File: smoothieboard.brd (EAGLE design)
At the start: 105.1 x 105.1 mm, 236 parts, among them IC1 LPC1769, IC10 LM1117-3.3V, IC11 78L12F, IC2 A4982, IC3 A4982, IC4 MCP44X1, IC5 A4982, IC6 A4982, J10 POWER_JACKSMD, J5 POWER_JACKSMD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

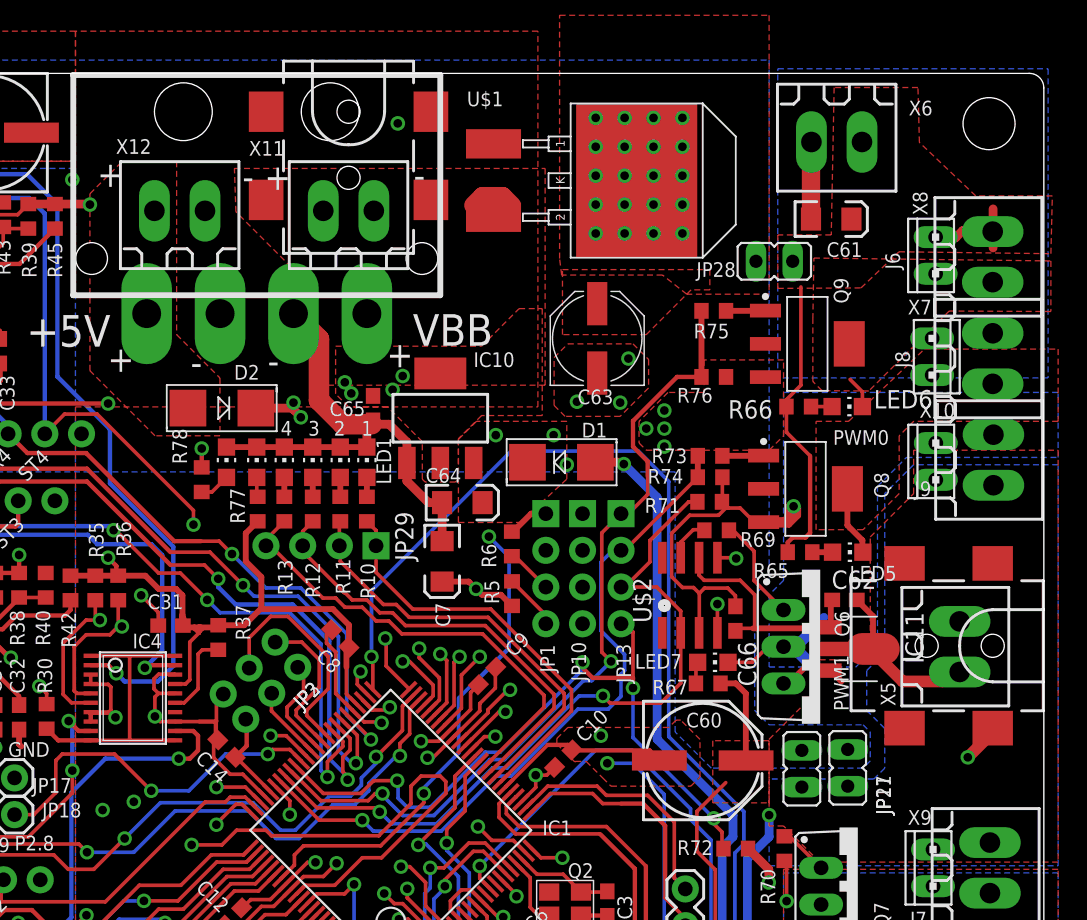
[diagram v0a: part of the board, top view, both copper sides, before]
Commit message: Removed Mosfet Driver Power SMD Jack
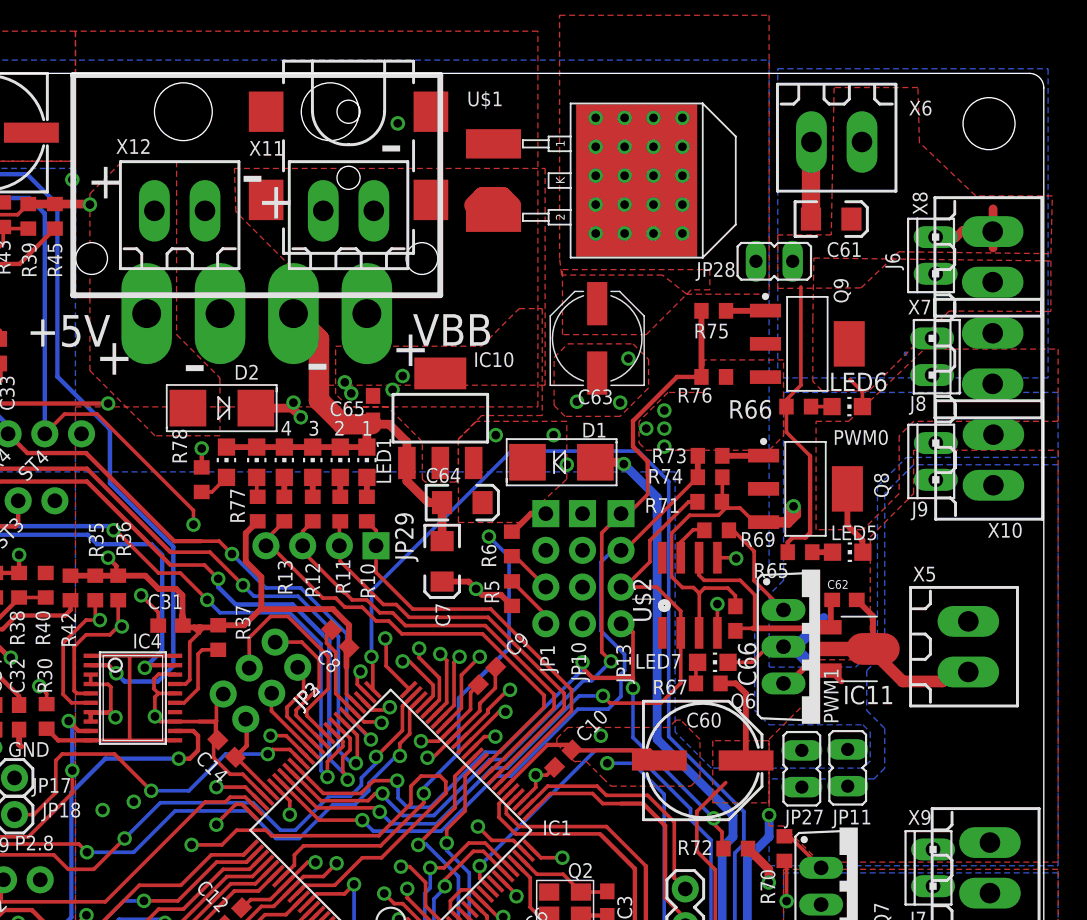
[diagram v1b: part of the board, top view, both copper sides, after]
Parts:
- removed J5: POWER_JACKSMD, SparkFun:POWER_JACK_SMD
- moved X5 0.60 mm to (99.8, 65.4)
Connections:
- net GND: no longer J5.VIN0
- net MOSFET_DRIVE: no longer J5.P$4
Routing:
- net GND: track 297.2 -> 294.4 mm, vias 234 -> 233

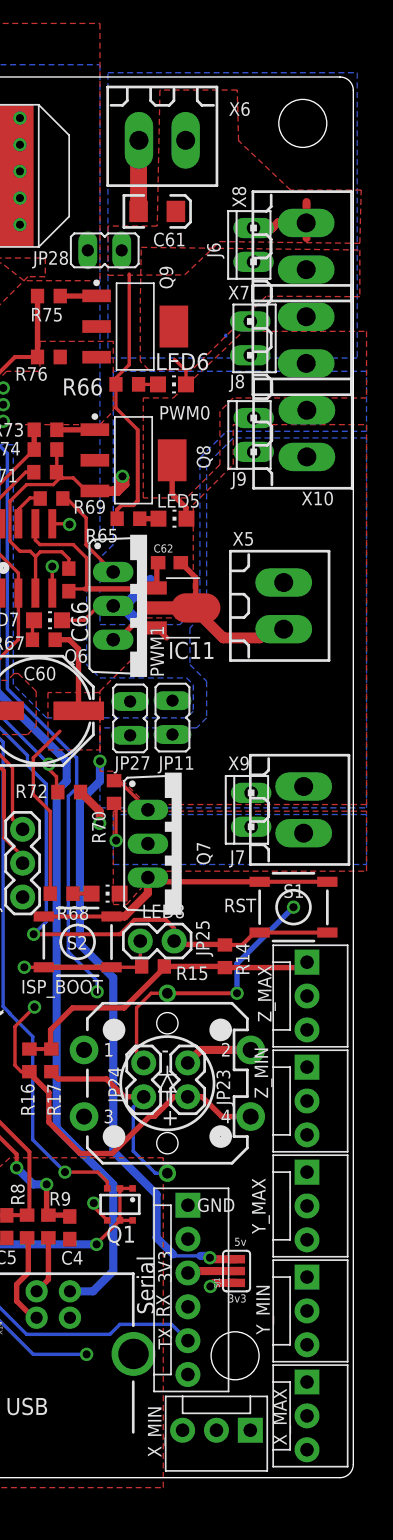
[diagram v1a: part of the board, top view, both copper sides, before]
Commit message: Removed second ground connection from IC11 (to improve MOSFET_DRIVE trace current handling)
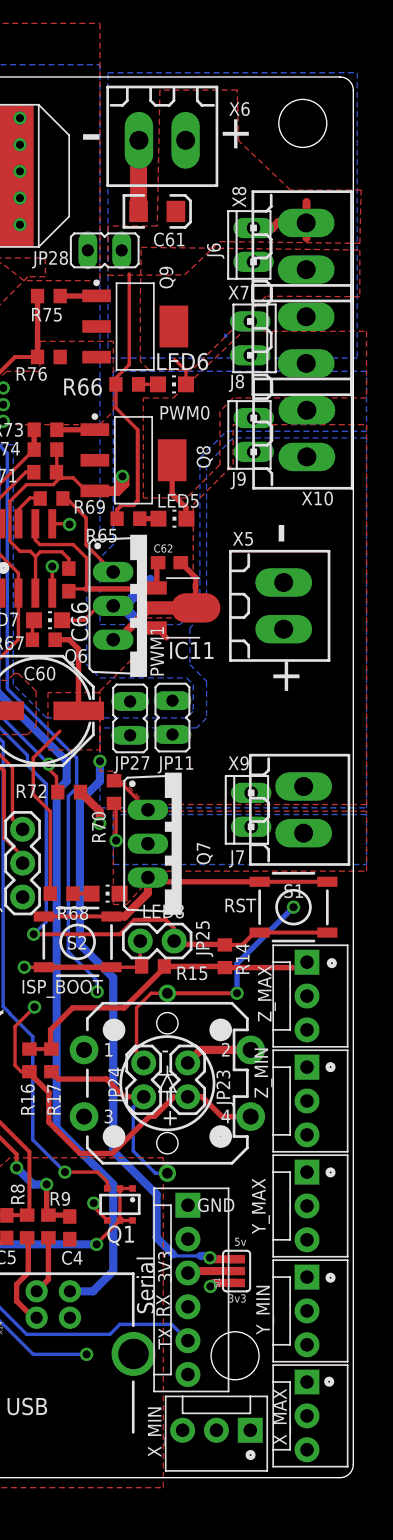
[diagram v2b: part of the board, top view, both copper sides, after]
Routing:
- net GND: track 294.4 -> 286.4 mm
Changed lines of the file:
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@@
 <setting verticaltext="up"/>
 </settings>
-<grid distance="0.1" unitdist="mm" unit="mm" style="dots" multiple="4" display="no" altdistance="0.0635" altunitdist="mm" altunit="mm"/>
+<grid distance="1" unitdist="mm" unit="mm" style="dots" multiple="4" display="no" altdistance="0.0635" altunitdist="mm" altunit="mm"/>
 <layers>
 <layer number="1" name="Top" color="4" fill="1" visible="yes" active="yes"/>
-<layer number="2" name="Route2" color="2" fill="1" visible="yes" active="yes"/>
+<layer number="2" name="Route2" color="2" fill="1" visible="no" active="yes"/>
 <layer number="3" name="Route3" color="4" fill="3" visible="no" active="no"/>
 <layer number="4" name="Route4" color="1" fill="4" visible="no" active="no"/>
@@
 <layer number="13" name="Route13" color="4" fill="5" visible="no" active="no"/>
 <layer number="14" name="Route14" color="1" fill="6" visible="no" active="no"/>
-<layer number="15" name="Route15" color="5" fill="1" visible="yes" active="yes"/>
+<layer number="15" name="Route15" color="5" fill="1" visible="no" active="yes"/>
 <layer number="16" name="Bottom" color="1" fill="1" visible="yes" active="yes"/>
 <layer number="17" name="Pads" color="2" fill="1" visible="yes" active="yes"/>
@@
 <text x="45.402" y="83.251" size="3.81" layer="25">-</text>
 <text x="53.902" y="83.351" size="3.81" layer="25">-</text>
+<circle x="97.3" y="1.7" radius="0.22360625" width="0.3048" layer="25"/>
+<circle x="103.2" y="7.2" radius="0.22360625" width="0.3048" layer="25"/>
+<circle x="103.3" y="15" radius="0.22360625" width="0.3048" layer="25"/>
+<circle x="103.3" y="22.9" radius="0.22360625" width="0.3048" layer="25"/>
+<circle x="103.3" y="30.8" radius="0.22360625" width="0.3048" layer="25"/>
+<circle x="103.4" y="38.6" radius="0.22360625" width="0.3048" layer="25"/>
+<text x="98.677" y="59.027" size="2.54" layer="25">+</text>
+<text x="101.049" y="70.002" size="3.81" layer="25" rot="R90">-</text>
+<text x="94.877" y="99.727" size="2.54" layer="25">+</text>
+<text x="84.502" y="99.151" size="3.81" layer="25">-</text>
 </plain>
 <attributes>
@@
 <wire x1="93.19" y1="65.25" x2="93.19" y2="67.5165" width="0.4064" layer="1"/>
 <wire x1="93.19" y1="67.5165" x2="92.0645" y2="68.642" width="0.4064" layer="1"/>
-<wire x1="93.19" y1="65.25" x2="93" y2="65.25" width="0.4064" layer="1"/>
-<wire x1="93" y1="65.25" x2="90.523" y2="65.25" width="0.4064" layer="1"/>
+<wire x1="93.19" y1="65.25" x2="90.523" y2="65.25" width="0.4064" layer="1"/>
 <wire x1="90.523" y1="65.25" x2="89.75" y2="65.25" width="0.4064" layer="1"/>
-<wire x1="89.75" y1="65.25" x2="87.365" y2="62.865" width="0.4064" layer="1"/>
-<wire x1="86.995" y1="62.865" x2="87.365" y2="62.865" width="0.4064" layer="1"/>
+<wire x1="89.75" y1="65.25" x2="87.365" y2="62.865" width="0.6096" layer="1"/>
+<wire x1="86.995" y1="62.865" x2="87.365" y2="62.865" width="0.6096" layer="1"/>
 <wire x1="68.58" y1="24.218" x2="68.58" y2="26.6065" width="0.6096" layer="1"/>
 <wire x1="68.58" y1="26.6065" x2="67.1195" y2="28.067" width="0.6096" layer="1"/>
@@
 <wire x1="85.979" y1="49.0855" x2="85.979" y2="49.999" width="0.6096" layer="1"/>
 <wire x1="85.979" y1="49.999" x2="84.543" y2="51.435" width="0.6096" layer="1"/>
-<wire x1="99.787" y1="63.655" x2="98.655" y2="63.655" width="0.8128" layer="1"/>
-<wire x1="98.655" y1="63.655" x2="98" y2="63" width="0.8128" layer="1"/>
-<wire x1="98" y1="63" x2="95.25" y2="63" width="0.8128" layer="1"/>
-<wire x1="95.25" y1="63" x2="93" y2="65.25" width="0.8128" layer="1"/>
 <via x="60.3045" y="101.619" extent="1-16" drill="0.6" diameter="1.016"/>
 <polygon width="0.8128" layer="1" rank="6">

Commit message: Fixed MOSFET labels on schematic to match BOM
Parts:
- Q6, Q7: value IRF540 -> AOT240L
- Q8, Q9: value BSP100 -> ZXMN4A06GTA
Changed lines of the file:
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@@
 <attribute name="VALUE" x="49.9745" y="73.406" size="1.27" layer="27" rot="R270"/>
 </element>
-<element name="Q6" library="transistor-power" package="TO220BV" value="IRF540" x="89.535" y="65.405" smashed="yes" rot="R270">
+<element name="Q6" library="transistor-power" package="TO220BV" value="AOT240L" x="89.535" y="65.405" smashed="yes" rot="R270">
 <attribute name="NAME" x="83.3185" y="61.1383" size="1.016" layer="25" ratio="10"/>
 <attribute name="VALUE" x="81.915" y="70.485" size="1.27" layer="27" ratio="10" rot="R270"/>
 </element>
-<element name="Q7" library="transistor-power" package="TO220BV" value="IRF540" x="92.1385" y="47.5615" smashed="yes" rot="R270">
+<element name="Q7" library="transistor-power" package="TO220BV" value="AOT240L" x="92.1385" y="47.5615" smashed="yes" rot="R270">
 <attribute name="NAME" x="93.2643" y="47.725" size="1.016" layer="25" ratio="10" rot="R270"/>
 <attribute name="VALUE" x="84.5185" y="52.6415" size="1.27" layer="27" ratio="10" rot="R270"/>
@@
 <attribute name="VALUE" x="50.9905" y="76.8985" size="1.27" layer="27" rot="R90"/>
 </element>
-<element name="Q8" library="ipc-7351-transistor" package="SOT230P700X160-4N" value="BSP100" x="88.519" y="76.327" smashed="yes">
+<element name="Q8" library="ipc-7351-transistor" package="SOT230P700X160-4N" value="ZXMN4A06GTA" x="88.519" y="76.327" smashed="yes">
 <attribute name="NAME" x="94.286" y="75.689" size="1.016" layer="25" font="vector" ratio="10" rot="R90"/>
 <attribute name="VALUE" x="87.0555" y="71.4895" size="1.27" layer="27" font="vector" ratio="10"/>
 </element>
-<element name="Q9" library="ipc-7351-transistor" package="SOT230P700X160-4N" value="BSP100" x="88.646" y="86.36" smashed="yes">
+<element name="Q9" library="ipc-7351-transistor" package="SOT230P700X160-4N" value="ZXMN4A06GTA" x="88.646" y="86.36" smashed="yes">
 <attribute name="NAME" x="91.492" y="89.151" size="1.016" layer="25" font="vector" ratio="10" rot="R90"/>
 <attribute name="VALUE" x="87.1825" y="81.5225" size="1.27" layer="27" font="vector" ratio="10"/>

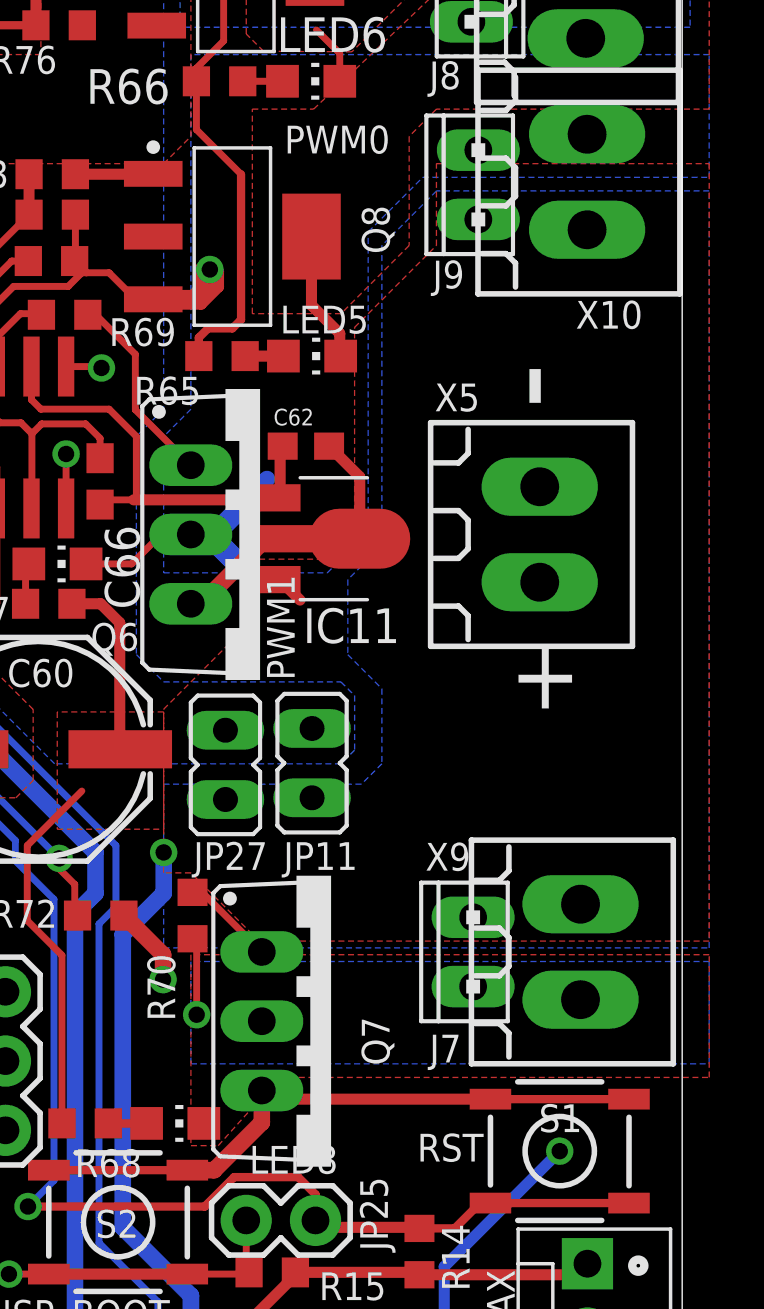
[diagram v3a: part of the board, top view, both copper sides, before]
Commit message: Changed Heated Bed connectors
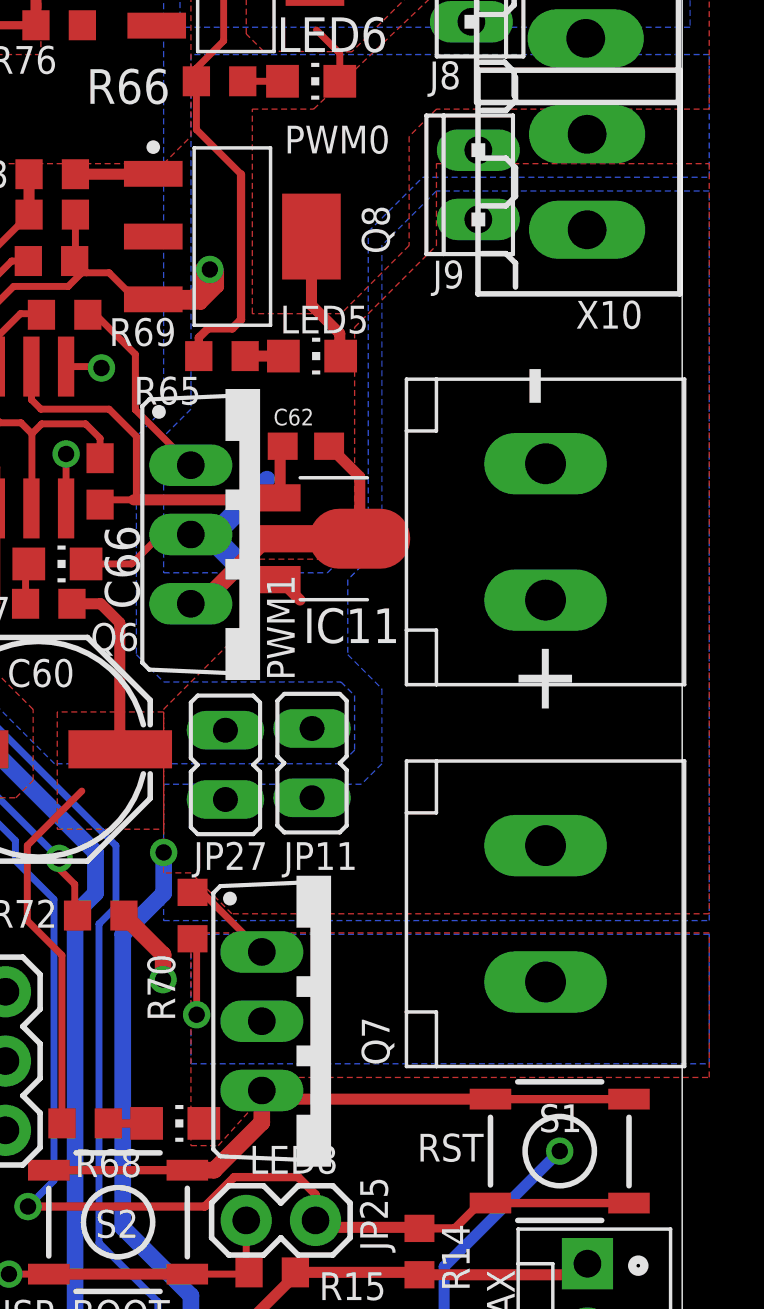
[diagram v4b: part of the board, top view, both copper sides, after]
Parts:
- removed J7: (no value), con-amp:10X02MTA
- removed X5, X9: (no value), con-weidmueller-sl35:180G-2
- added U$5, U$6: 5MMCONN, eric_sorensen:1715250000
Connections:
- net GND: now also U$5.P$2; no longer X5.2
- net MOSFET_DRIVE: now also U$5.P$1, U$6.P$2; no longer J7.1, X5.1, X9.1
- net N$94: now also U$6.P$1; no longer J7.2, X9.2
